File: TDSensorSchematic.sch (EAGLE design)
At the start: 13 parts, among them U1 MPL3115A2LGA8, U2 ADXL345PATRICK

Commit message: Update TDSensorSchematic.sch
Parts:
- removed JP1: (no value), SparkFun:M08
- removed JP4: (no value), SparkFun:M06SIP
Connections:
- removed net CS: JP1.3, U2.CS
- removed net N$3: C5.1, U1.CAP
- removed net SDO: JP1.6, U2.SDO
- removed net VCC: C1.1, C2.+, C3.1, C4.+, C6.1, CIO.1, JP1.2, JP4.5, R1.2, R2.2, U1.VDD, U1.VDDIO, U2.VDD, U2.VSS
- new net N$4: U1.GND
- new net VCC_3.3V: C1.1, C2.+, C3.1, C4.+, C6.1, CIO.1, R1.2, R2.2, U1.VDD, U1.VDDIO, U2.VDD, U2.VSS
- net GND: now also U1.CAP, U2.SDO; no longer JP4.6, U1.GND
- net INT1: no longer JP1.4, JP4.2, U2.INT1
- net INT2: no longer JP1.5, JP4.1, U2.INT2
- net SCL: no longer JP1.8, JP4.4, U2.SCL
- net SDA: no longer JP1.7, JP4.3
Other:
- note removed: "GND"
- note removed: "SCL"
- note removed: "SDA"
- note removed: "VCC"
- moved on the sheet: C1, C2, C3, C4, C5, C6, CIO, R2

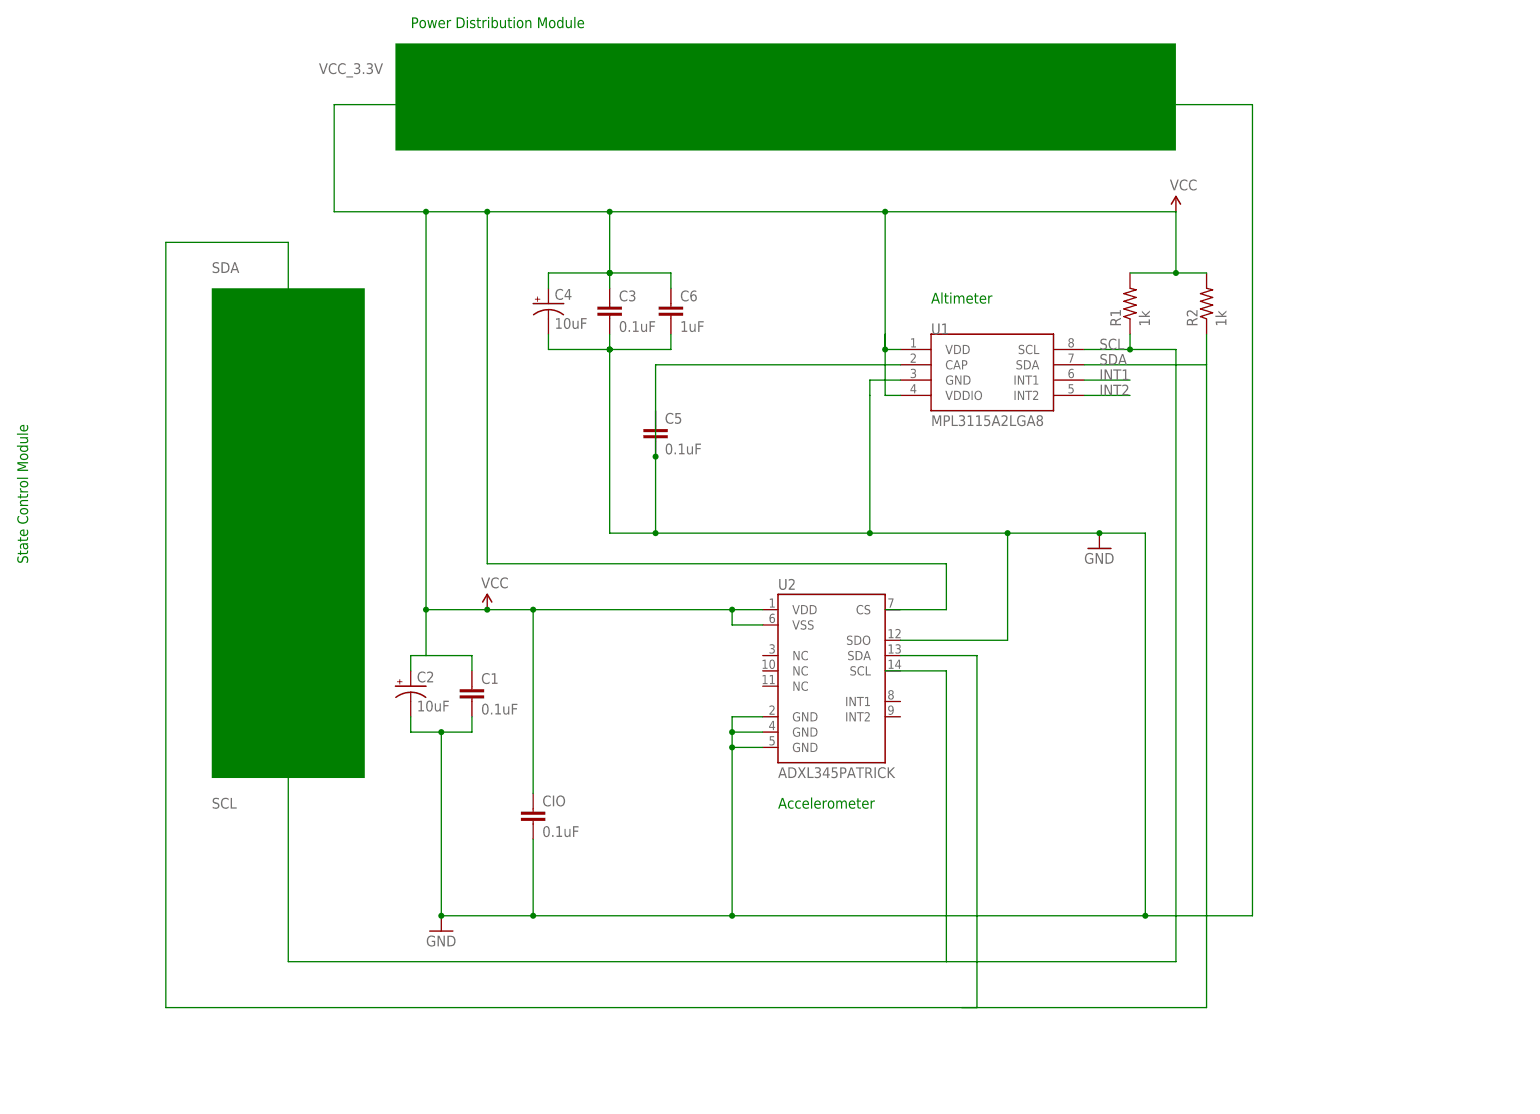
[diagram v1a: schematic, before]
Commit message: fixed ERC warnings
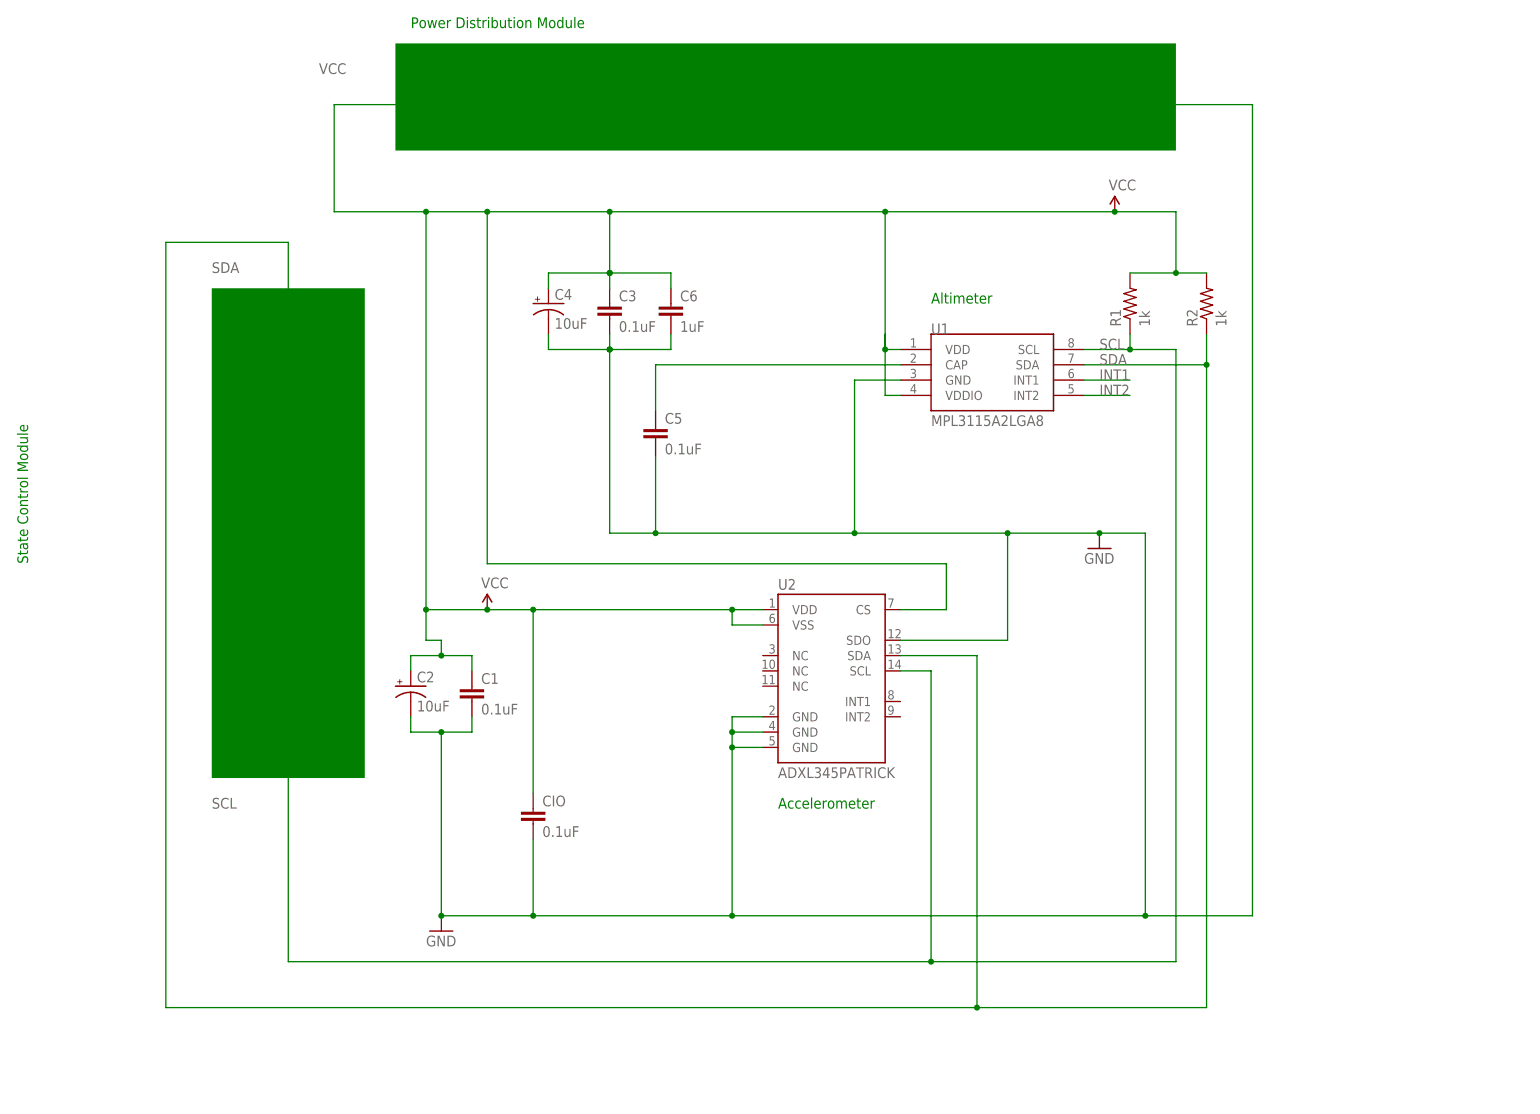
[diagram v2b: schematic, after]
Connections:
- removed net N$4: U1.GND
- removed net VCC_3.3V: C1.1, C2.+, C3.1, C4.+, C6.1, CIO.1, R1.2, R2.2, U1.VDD, U1.VDDIO, U2.VDD, U2.VSS
- new net N$1: C5.1, U1.CAP
- new net VCC: C1.1, C2.+, C3.1, C4.+, C6.1, CIO.1, R1.2, R2.2, U1.VDD, U1.VDDIO, U2.CS, U2.VDD, U2.VSS
- net GND: now also U1.GND; no longer U1.CAP
- net SCL: now also U2.SCL
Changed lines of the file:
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@@
 <part name="R1" library="SparkFun" deviceset="RESISTOR" device="0402-RES" value="1k"/>
 <part name="R2" library="SparkFun" deviceset="RESISTOR" device="0402-RES" value="1k"/>
-<part name="P+6" library="SparkFun" deviceset="VCC" device=""/>
 <part name="C4" library="SparkFun" deviceset="CAP_POL" device="1206" value="10uF"/>
 <part name="C5" library="SparkFun" deviceset="CAP" device="0402-CAP" value="0.1uF"/>
 <part name="GND5" library="SparkFun" deviceset="GND" device=""/>
 <part name="C6" library="SparkFun" deviceset="CAP" device="0402-CAP" value="1uF"/>
+<part name="P+1" library="SparkFun" deviceset="VCC" device=""/>
 </parts>
 <sheets>
@@
 <instance part="R1" gate="G$1" x="121.92" y="121.92" rot="R90"/>
 <instance part="R2" gate="G$1" x="134.62" y="121.92" rot="R90"/>
-<instance part="P+6" gate="1" x="129.54" y="137.16"/>
 <instance part="C4" gate="G$1" x="25.4" y="121.92"/>
 <instance part="C5" gate="G$1" x="43.18" y="99.06"/>
 <instance part="GND5" gate="1" x="116.84" y="81.28"/>
 <instance part="C6" gate="G$1" x="45.72" y="119.38"/>
+<instance part="P+1" gate="1" x="119.38" y="137.16"/>
 </instances>
 <busses>
@@
 <net name="GND" class="0">
 <segment>
-<wire x1="43.18" y1="111.76" x2="43.18" y2="96.52" width="0.1524" layer="91"/>
-<wire x1="43.18" y1="96.52" x2="43.18" y2="83.82" width="0.1524" layer="91"/>
-<wire x1="43.18" y1="83.82" x2="78.74" y2="83.82" width="0.1524" layer="91"/>
-<wire x1="78.74" y1="83.82" x2="101.6" y2="83.82" width="0.1524" layer="91"/>
+<wire x1="35.56" y1="83.82" x2="43.18" y2="83.82" width="0.1524" layer="91"/>
+<wire x1="43.18" y1="83.82" x2="76.2" y2="83.82" width="0.1524" layer="91"/>
+<wire x1="76.2" y1="83.82" x2="101.6" y2="83.82" width="0.1524" layer="91"/>
 <wire x1="101.6" y1="83.82" x2="116.84" y2="83.82" width="0.1524" layer="91"/>
 <wire x1="116.84" y1="83.82" x2="124.46" y2="83.82" width="0.1524" layer="91"/>
@@
 <wire x1="7.62" y1="20.32" x2="22.86" y2="20.32" width="0.1524" layer="91"/>
 <wire x1="22.86" y1="20.32" x2="55.88" y2="20.32" width="0.1524" layer="91"/>
-<wire x1="78.74" y1="106.68" x2="78.74" y2="83.82" width="0.1524" layer="91"/>
-<junction x="78.74" y="83.82"/>
 <wire x1="55.88" y1="53.34" x2="55.88" y2="50.8" width="0.1524" layer="91"/>
 <wire x1="55.88" y1="50.8" x2="55.88" y2="48.26" width="0.1524" layer="91"/>
@@
 <pinref part="C6" gate="G$1" pin="2"/>
 <wire x1="35.56" y1="114.3" x2="35.56" y2="83.82" width="0.1524" layer="91"/>
-<wire x1="35.56" y1="83.82" x2="43.18" y2="83.82" width="0.1524" layer="91"/>
-<junction x="43.18" y="83.82"/>
 <pinref part="U2" gate="G$1" pin="SDO"/>
 <wire x1="83.82" y1="66.04" x2="101.6" y2="66.04" width="0.1524" layer="91"/>
@@
 <junction x="7.62" y="20.32"/>
 <pinref part="C5" gate="G$1" pin="2"/>
-<junction x="43.18" y="96.52"/>
-<pinref part="U1" gate="G$1" pin="CAP"/>
-<wire x1="43.18" y1="111.76" x2="83.82" y2="111.76" width="0.1524" layer="91"/>
+<wire x1="43.18" y1="96.52" x2="43.18" y2="83.82" width="0.1524" layer="91"/>
+<junction x="43.18" y="83.82"/>
+<pinref part="U1" gate="G$1" pin="GND"/>
+<wire x1="83.82" y1="109.22" x2="76.2" y2="109.22" width="0.1524" layer="91"/>
+<wire x1="76.2" y1="109.22" x2="76.2" y2="83.82" width="0.1524" layer="91"/>
+<junction x="76.2" y="83.82"/>
 </segment>
 </net>
@@
 <junction x="121.92" y="114.3"/>
 <wire x1="-17.78" y1="43.18" x2="-17.78" y2="12.7" width="0.1524" layer="91"/>
-<wire x1="-17.78" y1="12.7" x2="91.44" y2="12.7" width="0.1524" layer="91"/>
-<wire x1="91.44" y1="12.7" x2="91.44" y2="60.96" width="0.1524" layer="91"/>
-<wire x1="91.44" y1="60.96" x2="81.28" y2="60.96" width="0.1524" layer="91"/>
-<wire x1="129.54" y1="12.7" x2="91.44" y2="12.7" width="0.1524" layer="91"/>
+<wire x1="-17.78" y1="12.7" x2="88.9" y2="12.7" width="0.1524" layer="91"/>
 <label x="-30.48" y="38.1" size="1.778" layer="95"/>
+<pinref part="U2" gate="G$1" pin="SCL"/>
+<wire x1="88.9" y1="12.7" x2="129.54" y2="12.7" width="0.1524" layer="91"/>
+<wire x1="83.82" y1="60.96" x2="88.9" y2="60.96" width="0.1524" layer="91"/>
+<wire x1="88.9" y1="60.96" x2="88.9" y2="12.7" width="0.1524" layer="91"/>
+<junction x="88.9" y="12.7"/>
 </segment>
 </net>
 <net name="SDA" class="0">
 <segment>
+<label x="116.84" y="111.76" size="1.778" layer="95"/>
+<pinref part="U1" gate="G$1" pin="SDA"/>
 <wire x1="96.52" y1="5.08" x2="-38.1" y2="5.08" width="0.1524" layer="91"/>
 <wire x1="-38.1" y1="5.08" x2="-38.1" y2="132.08" width="0.1524" layer="91"/>
@@
 <wire x1="96.52" y1="63.5" x2="96.52" y2="5.08" width="0.1524" layer="91"/>
 <label x="-30.48" y="127" size="1.778" layer="95"/>
-</segment>
-<segment>
+<wire x1="134.62" y1="5.08" x2="96.52" y2="5.08" width="0.1524" layer="91"/>
+<junction x="96.52" y="5.08"/>
+<pinref part="R2" gate="G$1" pin="1"/>
 <wire x1="134.62" y1="116.84" x2="134.62" y2="111.76" width="0.1524" layer="91"/>
-<wire x1="134.62" y1="111.76" x2="114.3" y2="111.76" width="0.1524" layer="91"/>
-<label x="116.84" y="111.76" size="1.778" layer="95"/>
-<pinref part="R2" gate="G$1" pin="1"/>
-<pinref part="U1" gate="G$1" pin="SDA"/>
+<wire x1="134.62" y1="111.76" x2="134.62" y2="5.08" width="0.1524" layer="91"/>
+<wire x1="114.3" y1="111.76" x2="134.62" y2="111.76" width="0.1524" layer="91"/>
+<junction x="134.62" y="111.76"/>
 </segment>
 </net>
@@
 </segment>
 </net>
-<net name="VCC_3.3V" class="0">
+<net name="N$1" class="0">
+<segment>
+<pinref part="C5" gate="G$1" pin="1"/>
+<wire x1="43.18" y1="104.14" x2="43.18" y2="111.76" width="0.1524" layer="91"/>
+<pinref part="U1" gate="G$1" pin="CAP"/>
+<wire x1="43.18" y1="111.76" x2="83.82" y2="111.76" width="0.1524" layer="91"/>
+</segment>
+</net>
+<net name="VCC" class="0">
 <segment>
 <wire x1="83.82" y1="114.3" x2="81.28" y2="114.3" width="0.1524" layer="91"/>
@@
 <pinref part="R1" gate="G$1" pin="2"/>
 <pinref part="R2" gate="G$1" pin="2"/>
-<pinref part="P+6" gate="1" pin="VCC"/>
 <wire x1="129.54" y1="127" x2="129.54" y2="137.16" width="0.1524" layer="91"/>
 <wire x1="-10.16" y1="137.16" x2="-10.16" y2="154.94" width="0.1524" layer="91"/>
@@
 <wire x1="15.24" y1="137.16" x2="5.08" y2="137.16" width="0.1524" layer="91"/>
 <wire x1="5.08" y1="137.16" x2="-10.16" y2="137.16" width="0.1524" layer="91"/>
-<wire x1="129.54" y1="137.16" x2="81.28" y2="137.16" width="0.1524" layer="91"/>
+<wire x1="129.54" y1="137.16" x2="119.38" y2="137.16" width="0.1524" layer="91"/>
+<wire x1="119.38" y1="137.16" x2="81.28" y2="137.16" width="0.1524" layer="91"/>
 <wire x1="81.28" y1="114.3" x2="81.28" y2="137.16" width="0.1524" layer="91"/>
 <junction x="81.28" y="137.16"/>
 <wire x1="129.54" y1="127" x2="121.92" y2="127" width="0.1524" layer="91"/>
-<wire x1="2.54" y1="60.96" x2="2.54" y2="63.5" width="0.1524" layer="91"/>
-<wire x1="12.7" y1="60.96" x2="12.7" y2="63.5" width="0.1524" layer="91"/>
-<wire x1="12.7" y1="63.5" x2="5.08" y2="63.5" width="0.1524" layer="91"/>
-<pinref part="C2" gate="G$1" pin="+"/>
-<pinref part="C1" gate="G$1" pin="1"/>
-<wire x1="5.08" y1="63.5" x2="2.54" y2="63.5" width="0.1524" layer="91"/>
-<wire x1="5.08" y1="63.5" x2="5.08" y2="71.12" width="0.1524" layer="91"/>
 <junction x="5.08" y="137.16"/>
 <pinref part="CIO" gate="G$1" pin="1"/>
@@
 <wire x1="22.86" y1="40.64" x2="22.86" y2="71.12" width="0.1524" layer="91"/>
 <wire x1="22.86" y1="71.12" x2="15.24" y2="71.12" width="0.1524" layer="91"/>
-<junction x="5.08" y="71.12"/>
 <wire x1="15.24" y1="71.12" x2="5.08" y2="71.12" width="0.1524" layer="91"/>
 <wire x1="60.96" y1="68.58" x2="55.88" y2="68.58" width="0.1524" layer="91"/>
@@
 <junction x="35.56" y="137.16"/>
 <label x="-12.7" y="160.02" size="1.778" layer="95"/>
-<wire x1="81.28" y1="71.12" x2="91.44" y2="71.12" width="0.1524" layer="91"/>
 <wire x1="91.44" y1="71.12" x2="91.44" y2="78.74" width="0.1524" layer="91"/>
 <wire x1="91.44" y1="78.74" x2="15.24" y2="78.74" width="0.1524" layer="91"/>
 <wire x1="15.24" y1="78.74" x2="15.24" y2="137.16" width="0.1524" layer="91"/>
 <junction x="15.24" y="137.16"/>
-</segment>
-</net>
-<net name="N$4" class="0">
-<segment>
-<wire x1="83.82" y1="109.22" x2="78.74" y2="109.22" width="0.1524" layer="91"/>
-<wire x1="78.74" y1="109.22" x2="78.74" y2="106.68" width="0.1524" layer="91"/>
-<pinref part="U1" gate="G$1" pin="GND"/>
-</segment>
-</net>
-<net name="N$6" class="0">
-<segment>
-<wire x1="134.62" y1="5.08" x2="93.98" y2="5.08" width="0.1524" layer="91"/>
-<wire x1="134.62" y1="111.76" x2="134.62" y2="5.08" width="0.1524" layer="91"/>
+<pinref part="U2" gate="G$1" pin="CS"/>
+<wire x1="83.82" y1="71.12" x2="91.44" y2="71.12" width="0.1524" layer="91"/>
+<pinref part="P+1" gate="1" pin="VCC"/>
+<junction x="119.38" y="137.16"/>
+<pinref part="C1" gate="G$1" pin="1"/>
+<wire x1="12.7" y1="60.96" x2="12.7" y2="63.5" width="0.1524" layer="91"/>
+<wire x1="12.7" y1="63.5" x2="7.62" y2="63.5" width="0.1524" layer="91"/>
+<wire x1="7.62" y1="63.5" x2="2.54" y2="63.5" width="0.1524" layer="91"/>
+<wire x1="2.54" y1="60.96" x2="2.54" y2="63.5" width="0.1524" layer="91"/>
+<pinref part="C2" gate="G$1" pin="+"/>
+<wire x1="5.08" y1="66.04" x2="7.62" y2="66.04" width="0.1524" layer="91"/>
+<wire x1="7.62" y1="66.04" x2="7.62" y2="63.5" width="0.1524" layer="91"/>
+<junction x="7.62" y="63.5"/>
+<wire x1="5.08" y1="66.04" x2="5.08" y2="71.12" width="0.1524" layer="91"/>
+<junction x="5.08" y="71.12"/>
 </segment>
 </net>
@@
 </sheet>
 </sheets>
+<errors>
+</errors>
 </schematic>
 </drawing>
